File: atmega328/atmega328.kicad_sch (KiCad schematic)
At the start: 11 parts, among them SW3 SW_SPST, SW4 SW_SPST, U16 ATmega328-A, U17 HEADER_3x2, Y4 Crystal_GND2

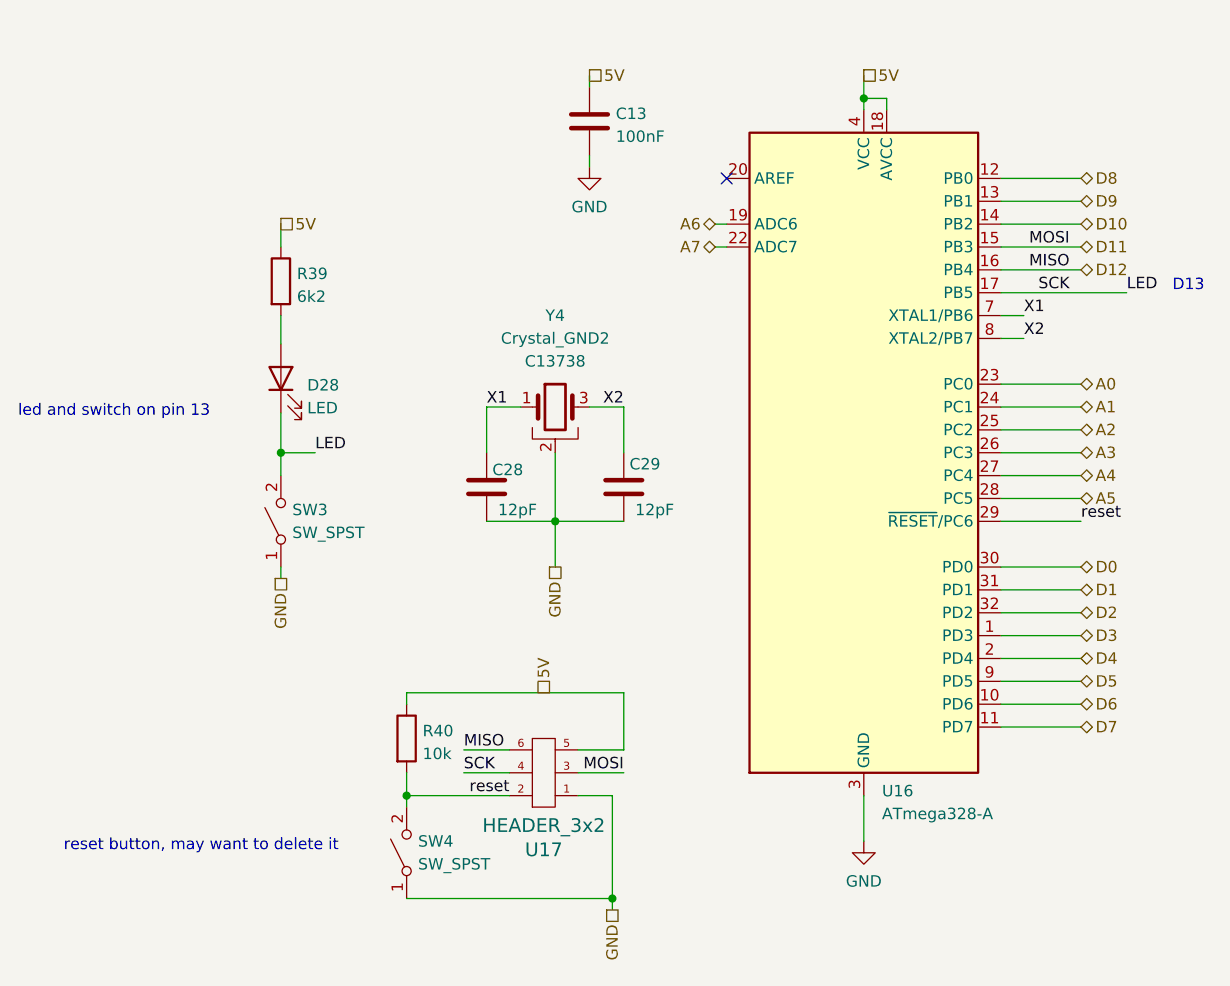
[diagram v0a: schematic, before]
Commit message: moved some schematic scheets to their own folders and routed a board with it. This allow for re-use of PCB parts.
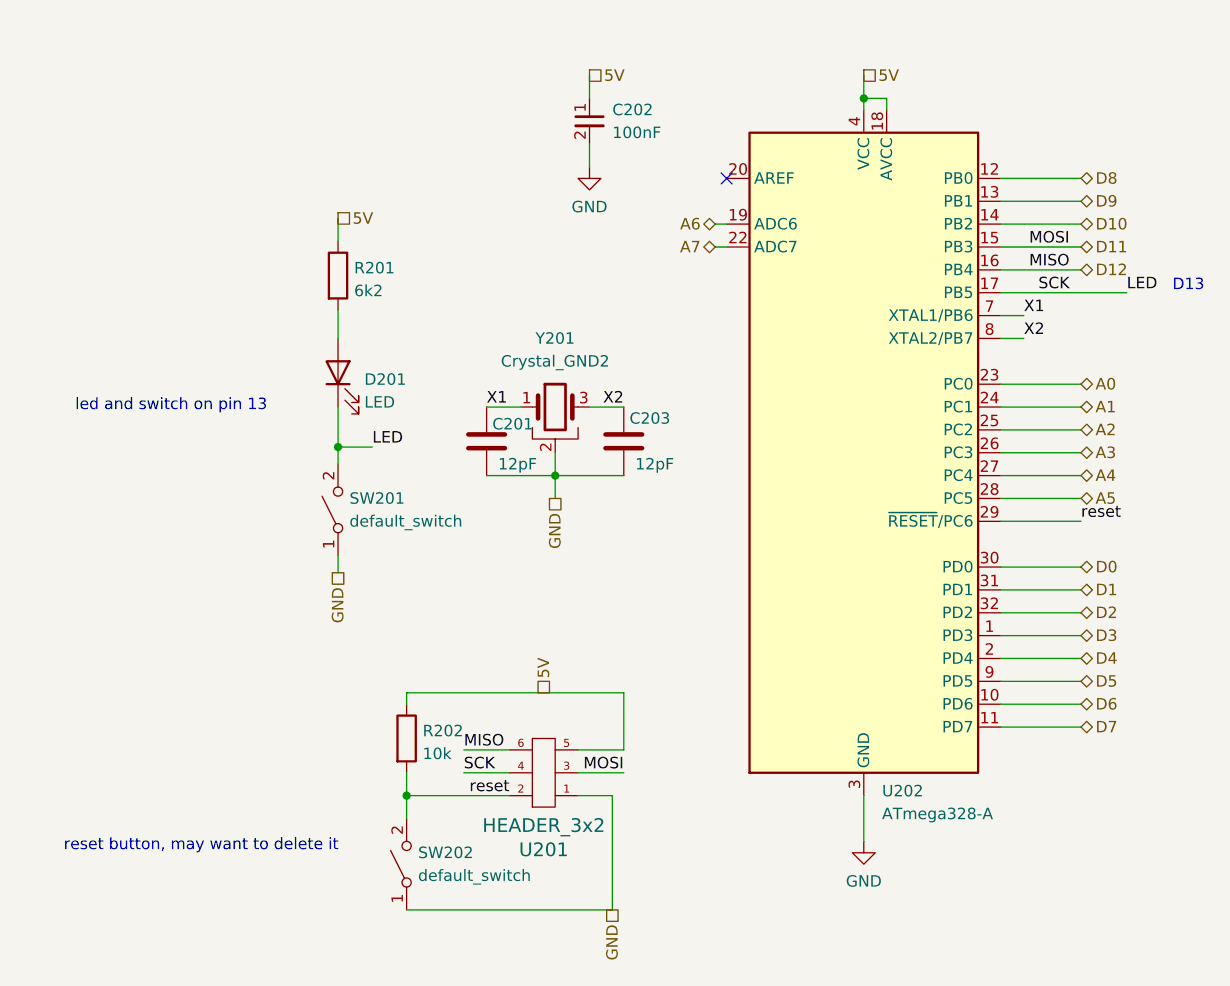
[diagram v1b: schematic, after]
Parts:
- removed C13: 100nF, Capacitor_SMD:C_0603_1608Metric_Pad1.08x0.95mm_HandSolder, symbol Device:C
- removed SW3, SW4: SW_SPST, Button_Switch_SMD:SW_SPST_SKQG_WithStem, symbol Switch:SW_SPST
- added C202: 100nF, Capacitor_SMD:C_0402_1005Metric, symbol capacitor_miscellaneous:C_0402_100nF
- added SW201, SW202: default_switch, custom_kicad_lib_sk:default_switch, symbol custom_kicad_lib_sk:default_switch
- C201: renamed from C28; footprint Capacitor_SMD:C_0805_2012Metric_Pad1.18x1.45mm_HandSolder -> Capacitor_SMD:C_0603_1608Metric; JLCPCB Part# (none) -> C38523
- C203: renamed from C29; footprint Capacitor_SMD:C_0805_2012Metric_Pad1.18x1.45mm_HandSolder -> Capacitor_SMD:C_0603_1608Metric; JLCPCB Part# C1792 -> C38523
- renumbered D28 to D201, R39 to R201, R40 to R202, U17 to U201, U16 to U202, Y4 to Y201
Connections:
- net 5V: now also C202.1
- net GND: now also C202.2, SW201.1 (A), SW202.1 (A)
- net LED: now also SW201.2 (B)
- net reset: now also SW202.2 (B)
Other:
- moved on the sheet: C201, C203, D201, R201

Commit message: removed hierarchial labels for power symbols and replaced them with actual power symbols also updated footprint of the inductor of the 5V buck
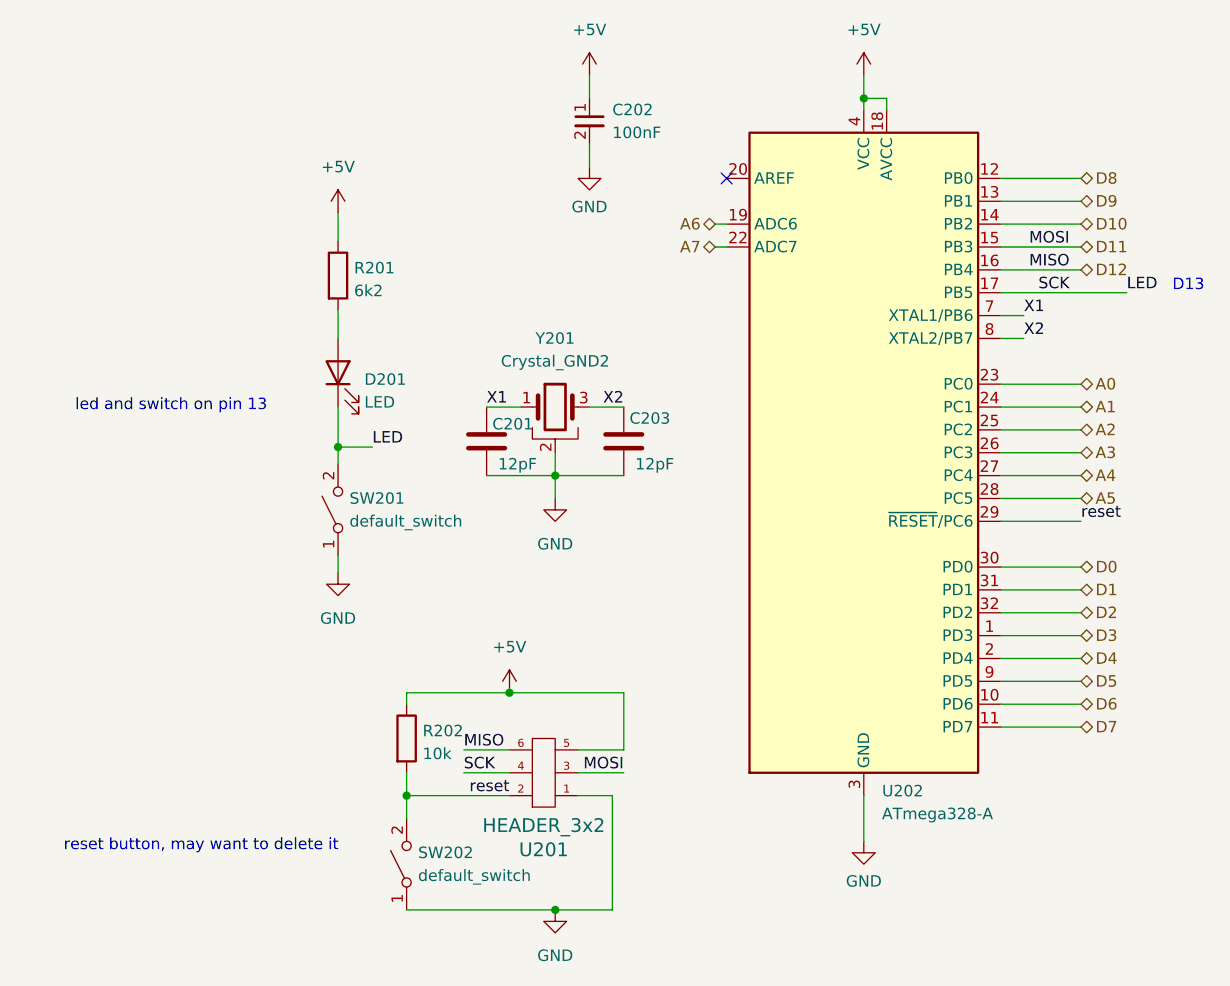
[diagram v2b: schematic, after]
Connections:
- net 5V renamed +5V
